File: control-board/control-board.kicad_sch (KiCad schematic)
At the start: 63 parts, among them J1 LED ch 1-24, J10 ESP32 left (3V3 row), J11 ESP32 right (GND row), J2 LED ch 25-48, J3 LED ch 49-72, J4 LED ch 73-96, J5 logic/analog, J6 24V IN, J7 24V IN (5.5/2.5), J8 FAN 24V, Q1 AO3400A, SW1 MODE, SW2 UP, SW3 DOWN, U101 PCA9685PW (0x40), U102 PCA9685PW (0x41), U103 PCA9685PW (0x42), U104 PCA9685PW (0x43), U105 PCA9685PW (0x44), U106 PCA9685PW (0x45), U110 XL1509-5.0E1, U111 ADS1115IDGS (DNP)

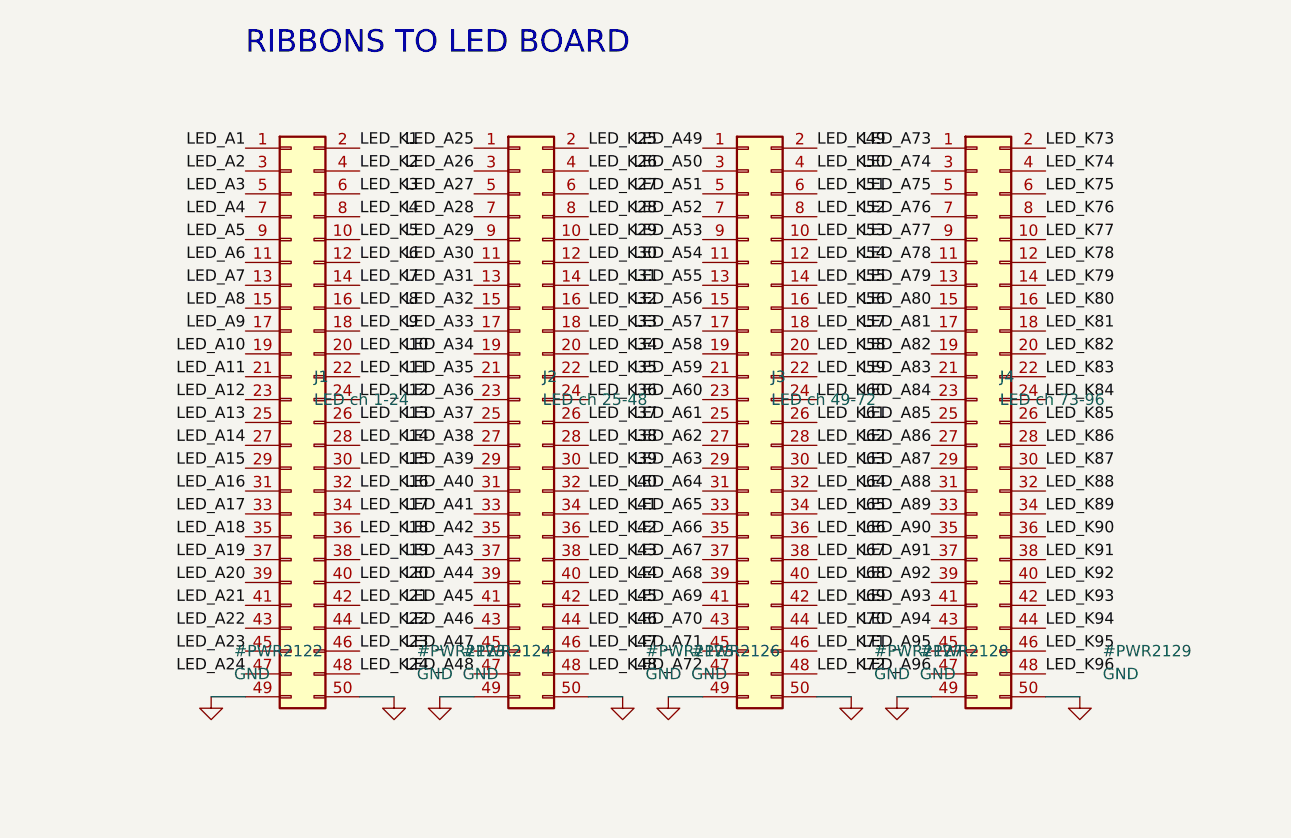
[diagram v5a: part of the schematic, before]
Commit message: Optimize ribbon/mux pin assignments to match user's PCB placement
- Quadrant mapping from actual footprint positions (via pcbnew API):
  J1 left-back = cols1-6/rows1-4, J2 right-back = cols7-12/rows1-4,
  J4 left-front = cols1-6/rows5-8, J3 right-front = cols7-12/rows5-8;
  pin pairs column-major in physical pin-1 direction (nested fan-out,
  no crossings)
- NTC->mux side-matched: U1-U3 serve cols 1-6, U6/U5/U4 cols 7-12
- pin_maps.py generated by optimize_pins.py; design_data now table-driven
- 274 labels renamed in the hand-edited LED sch (proximity-matched,
  0 misses); control board regenerated; CONNECTIONS.md updated
- Both netlists verify (300+412 nets), LED ERC still 0 errors

Co-Authored-By: Claude Fable 5 <noreply@anthropic.com>
Claude-Session: https://claude.ai/code/session_017oD54uh7Tvu54u9NPQNcZB
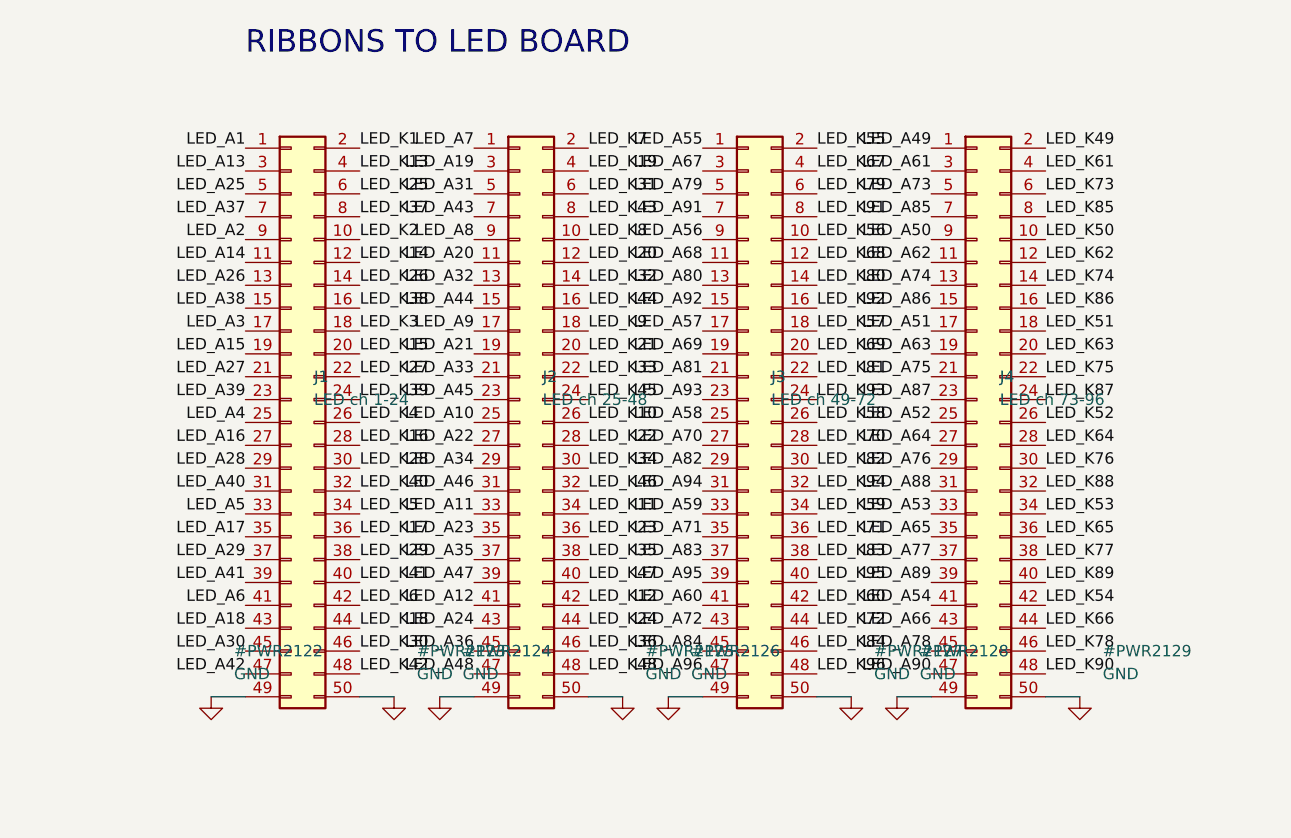
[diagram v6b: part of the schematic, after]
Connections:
- net LED_A10: now also J2.25 (Pin_25); no longer J1.19 (Pin_19)
- net LED_A11: now also J2.33 (Pin_33); no longer J1.21 (Pin_21)
- net LED_A12: now also J2.41 (Pin_41); no longer J1.23 (Pin_23)
- net LED_A13: now also J1.3 (Pin_3); no longer J1.25 (Pin_25)
- net LED_A14: now also J1.11 (Pin_11); no longer J1.27 (Pin_27)
- net LED_A15: now also J1.19 (Pin_19); no longer J1.29 (Pin_29)
- net LED_A16: now also J1.27 (Pin_27); no longer J1.31 (Pin_31)
- net LED_A17: now also J1.35 (Pin_35); no longer J1.33 (Pin_33)
- net LED_A18: now also J1.43 (Pin_43); no longer J1.35 (Pin_35)
- net LED_A19: now also J2.3 (Pin_3); no longer J1.37 (Pin_37)
- net LED_A2: now also J1.9 (Pin_9); no longer J1.3 (Pin_3)
- net LED_A20: now also J2.11 (Pin_11); no longer J1.39 (Pin_39)
- net LED_A21: now also J2.19 (Pin_19); no longer J1.41 (Pin_41)
- net LED_A22: now also J2.27 (Pin_27); no longer J1.43 (Pin_43)
- net LED_A23: now also J2.35 (Pin_35); no longer J1.45 (Pin_45)
- net LED_A24: now also J2.43 (Pin_43); no longer J1.47 (Pin_47)
- net LED_A25: now also J1.5 (Pin_5); no longer J2.1 (Pin_1)
- net LED_A26: now also J1.13 (Pin_13); no longer J2.3 (Pin_3)
- net LED_A27: now also J1.21 (Pin_21); no longer J2.5 (Pin_5)
- net LED_A28: now also J1.29 (Pin_29); no longer J2.7 (Pin_7)
- net LED_A29: now also J1.37 (Pin_37); no longer J2.9 (Pin_9)
- net LED_A3: now also J1.17 (Pin_17); no longer J1.5 (Pin_5)
- net LED_A30: now also J1.45 (Pin_45); no longer J2.11 (Pin_11)
- net LED_A31: now also J2.5 (Pin_5); no longer J2.13 (Pin_13)
- net LED_A32: now also J2.13 (Pin_13); no longer J2.15 (Pin_15)
- net LED_A33: now also J2.21 (Pin_21); no longer J2.17 (Pin_17)
- net LED_A34: now also J2.29 (Pin_29); no longer J2.19 (Pin_19)
- net LED_A35: now also J2.37 (Pin_37); no longer J2.21 (Pin_21)
- net LED_A36: now also J2.45 (Pin_45); no longer J2.23 (Pin_23)
- net LED_A37: now also J1.7 (Pin_7); no longer J2.25 (Pin_25)
- net LED_A38: now also J1.15 (Pin_15); no longer J2.27 (Pin_27)
- net LED_A39: now also J1.23 (Pin_23); no longer J2.29 (Pin_29)
- net LED_A4: now also J1.25 (Pin_25); no longer J1.7 (Pin_7)
- net LED_A40: now also J1.31 (Pin_31); no longer J2.31 (Pin_31)
- net LED_A41: now also J1.39 (Pin_39); no longer J2.33 (Pin_33)
- net LED_A42: now also J1.47 (Pin_47); no longer J2.35 (Pin_35)
- net LED_A43: now also J2.7 (Pin_7); no longer J2.37 (Pin_37)
- net LED_A44: now also J2.15 (Pin_15); no longer J2.39 (Pin_39)
- net LED_A45: now also J2.23 (Pin_23); no longer J2.41 (Pin_41)
- net LED_A46: now also J2.31 (Pin_31); no longer J2.43 (Pin_43)
- net LED_A47: now also J2.39 (Pin_39); no longer J2.45 (Pin_45)
- net LED_A49: now also J4.1 (Pin_1); no longer J3.1 (Pin_1)
- net LED_A5: now also J1.33 (Pin_33); no longer J1.9 (Pin_9)
- net LED_A50: now also J4.9 (Pin_9); no longer J3.3 (Pin_3)
- net LED_A51: now also J4.17 (Pin_17); no longer J3.5 (Pin_5)
- net LED_A52: now also J4.25 (Pin_25); no longer J3.7 (Pin_7)
- net LED_A53: now also J4.33 (Pin_33); no longer J3.9 (Pin_9)
- net LED_A54: now also J4.41 (Pin_41); no longer J3.11 (Pin_11)
- net LED_A55: now also J3.1 (Pin_1); no longer J3.13 (Pin_13)
- net LED_A56: now also J3.9 (Pin_9); no longer J3.15 (Pin_15)
- net LED_A58: now also J3.25 (Pin_25); no longer J3.19 (Pin_19)
- net LED_A59: now also J3.33 (Pin_33); no longer J3.21 (Pin_21)
- net LED_A6: now also J1.41 (Pin_41); no longer J1.11 (Pin_11)
- net LED_A60: now also J3.41 (Pin_41); no longer J3.23 (Pin_23)
- net LED_A61: now also J4.3 (Pin_3); no longer J3.25 (Pin_25)
- net LED_A62: now also J4.11 (Pin_11); no longer J3.27 (Pin_27)
- net LED_A63: now also J4.19 (Pin_19); no longer J3.29 (Pin_29)
- net LED_A64: now also J4.27 (Pin_27); no longer J3.31 (Pin_31)
- net LED_A65: now also J4.35 (Pin_35); no longer J3.33 (Pin_33)
- net LED_A66: now also J4.43 (Pin_43); no longer J3.35 (Pin_35)
- net LED_A67: now also J3.3 (Pin_3); no longer J3.37 (Pin_37)
- net LED_A68: now also J3.11 (Pin_11); no longer J3.39 (Pin_39)
- net LED_A69: now also J3.19 (Pin_19); no longer J3.41 (Pin_41)
- net LED_A7: now also J2.1 (Pin_1); no longer J1.13 (Pin_13)
- net LED_A70: now also J3.27 (Pin_27); no longer J3.43 (Pin_43)
- net LED_A71: now also J3.35 (Pin_35); no longer J3.45 (Pin_45)
- net LED_A72: now also J3.43 (Pin_43); no longer J3.47 (Pin_47)
- net LED_A73: now also J4.5 (Pin_5); no longer J4.1 (Pin_1)
- net LED_A74: now also J4.13 (Pin_13); no longer J4.3 (Pin_3)
- net LED_A75: now also J4.21 (Pin_21); no longer J4.5 (Pin_5)
- net LED_A76: now also J4.29 (Pin_29); no longer J4.7 (Pin_7)
- net LED_A77: now also J4.37 (Pin_37); no longer J4.9 (Pin_9)
- net LED_A78: now also J4.45 (Pin_45); no longer J4.11 (Pin_11)
- net LED_A79: now also J3.5 (Pin_5); no longer J4.13 (Pin_13)
- net LED_A8: now also J2.9 (Pin_9); no longer J1.15 (Pin_15)
- net LED_A80: now also J3.13 (Pin_13); no longer J4.15 (Pin_15)
- net LED_A81: now also J3.21 (Pin_21); no longer J4.17 (Pin_17)
- net LED_A82: now also J3.29 (Pin_29); no longer J4.19 (Pin_19)
- net LED_A83: now also J3.37 (Pin_37); no longer J4.21 (Pin_21)
- net LED_A84: now also J3.45 (Pin_45); no longer J4.23 (Pin_23)
- net LED_A85: now also J4.7 (Pin_7); no longer J4.25 (Pin_25)
- net LED_A86: now also J4.15 (Pin_15); no longer J4.27 (Pin_27)
- net LED_A87: now also J4.23 (Pin_23); no longer J4.29 (Pin_29)
- net LED_A89: now also J4.39 (Pin_39); no longer J4.33 (Pin_33)
- net LED_A9: now also J2.17 (Pin_17); no longer J1.17 (Pin_17)
- net LED_A90: now also J4.47 (Pin_47); no longer J4.35 (Pin_35)
- net LED_A91: now also J3.7 (Pin_7); no longer J4.37 (Pin_37)
- net LED_A92: now also J3.15 (Pin_15); no longer J4.39 (Pin_39)
- net LED_A93: now also J3.23 (Pin_23); no longer J4.41 (Pin_41)
- net LED_A94: now also J3.31 (Pin_31); no longer J4.43 (Pin_43)
- net LED_A95: now also J3.39 (Pin_39); no longer J4.45 (Pin_45)
- net LED_A96: now also J3.47 (Pin_47); no longer J4.47 (Pin_47)
- net LED_K10: now also J2.26 (Pin_26); no longer J1.20 (Pin_20)
- net LED_K11: now also J2.34 (Pin_34); no longer J1.22 (Pin_22)
- net LED_K12: now also J2.42 (Pin_42); no longer J1.24 (Pin_24)
- net LED_K13: now also J1.4 (Pin_4); no longer J1.26 (Pin_26)
- net LED_K14: now also J1.12 (Pin_12); no longer J1.28 (Pin_28)
- net LED_K15: now also J1.20 (Pin_20); no longer J1.30 (Pin_30)
- net LED_K16: now also J1.28 (Pin_28); no longer J1.32 (Pin_32)
- net LED_K17: now also J1.36 (Pin_36); no longer J1.34 (Pin_34)
- net LED_K18: now also J1.44 (Pin_44); no longer J1.36 (Pin_36)
- net LED_K19: now also J2.4 (Pin_4); no longer J1.38 (Pin_38)
- net LED_K2: now also J1.10 (Pin_10); no longer J1.4 (Pin_4)
- net LED_K20: now also J2.12 (Pin_12); no longer J1.40 (Pin_40)
- net LED_K21: now also J2.20 (Pin_20); no longer J1.42 (Pin_42)
- net LED_K22: now also J2.28 (Pin_28); no longer J1.44 (Pin_44)
- net LED_K23: now also J2.36 (Pin_36); no longer J1.46 (Pin_46)
- net LED_K24: now also J2.44 (Pin_44); no longer J1.48 (Pin_48)
- net LED_K25: now also J1.6 (Pin_6); no longer J2.2 (Pin_2)
- net LED_K26: now also J1.14 (Pin_14); no longer J2.4 (Pin_4)
- net LED_K27: now also J1.22 (Pin_22); no longer J2.6 (Pin_6)
- net LED_K28: now also J1.30 (Pin_30); no longer J2.8 (Pin_8)
- net LED_K29: now also J1.38 (Pin_38); no longer J2.10 (Pin_10)
- net LED_K3: now also J1.18 (Pin_18); no longer J1.6 (Pin_6)
- net LED_K30: now also J1.46 (Pin_46); no longer J2.12 (Pin_12)
- net LED_K31: now also J2.6 (Pin_6); no longer J2.14 (Pin_14)
- net LED_K32: now also J2.14 (Pin_14); no longer J2.16 (Pin_16)
- net LED_K33: now also J2.22 (Pin_22); no longer J2.18 (Pin_18)
- net LED_K34: now also J2.30 (Pin_30); no longer J2.20 (Pin_20)
- net LED_K35: now also J2.38 (Pin_38); no longer J2.22 (Pin_22)
- net LED_K36: now also J2.46 (Pin_46); no longer J2.24 (Pin_24)
- net LED_K37: now also J1.8 (Pin_8); no longer J2.26 (Pin_26)
- net LED_K38: now also J1.16 (Pin_16); no longer J2.28 (Pin_28)
- net LED_K39: now also J1.24 (Pin_24); no longer J2.30 (Pin_30)
- net LED_K4: now also J1.26 (Pin_26); no longer J1.8 (Pin_8)
- net LED_K40: now also J1.32 (Pin_32); no longer J2.32 (Pin_32)
- net LED_K41: now also J1.40 (Pin_40); no longer J2.34 (Pin_34)
- net LED_K42: now also J1.48 (Pin_48); no longer J2.36 (Pin_36)
- net LED_K43: now also J2.8 (Pin_8); no longer J2.38 (Pin_38)
- net LED_K44: now also J2.16 (Pin_16); no longer J2.40 (Pin_40)
- net LED_K45: now also J2.24 (Pin_24); no longer J2.42 (Pin_42)
- net LED_K46: now also J2.32 (Pin_32); no longer J2.44 (Pin_44)
- net LED_K47: now also J2.40 (Pin_40); no longer J2.46 (Pin_46)
- net LED_K49: now also J4.2 (Pin_2); no longer J3.2 (Pin_2)
- net LED_K5: now also J1.34 (Pin_34); no longer J1.10 (Pin_10)
- net LED_K50: now also J4.10 (Pin_10); no longer J3.4 (Pin_4)
- net LED_K51: now also J4.18 (Pin_18); no longer J3.6 (Pin_6)
- net LED_K52: now also J4.26 (Pin_26); no longer J3.8 (Pin_8)
- net LED_K53: now also J4.34 (Pin_34); no longer J3.10 (Pin_10)
- net LED_K54: now also J4.42 (Pin_42); no longer J3.12 (Pin_12)
- net LED_K55: now also J3.2 (Pin_2); no longer J3.14 (Pin_14)
- net LED_K56: now also J3.10 (Pin_10); no longer J3.16 (Pin_16)
- net LED_K58: now also J3.26 (Pin_26); no longer J3.20 (Pin_20)
- net LED_K59: now also J3.34 (Pin_34); no longer J3.22 (Pin_22)
- net LED_K6: now also J1.42 (Pin_42); no longer J1.12 (Pin_12)
- net LED_K60: now also J3.42 (Pin_42); no longer J3.24 (Pin_24)
- net LED_K61: now also J4.4 (Pin_4); no longer J3.26 (Pin_26)
- net LED_K62: now also J4.12 (Pin_12); no longer J3.28 (Pin_28)
- net LED_K63: now also J4.20 (Pin_20); no longer J3.30 (Pin_30)
- net LED_K64: now also J4.28 (Pin_28); no longer J3.32 (Pin_32)
- net LED_K65: now also J4.36 (Pin_36); no longer J3.34 (Pin_34)
- net LED_K66: now also J4.44 (Pin_44); no longer J3.36 (Pin_36)
- net LED_K67: now also J3.4 (Pin_4); no longer J3.38 (Pin_38)
- net LED_K68: now also J3.12 (Pin_12); no longer J3.40 (Pin_40)
- net LED_K69: now also J3.20 (Pin_20); no longer J3.42 (Pin_42)
- net LED_K7: now also J2.2 (Pin_2); no longer J1.14 (Pin_14)
- net LED_K70: now also J3.28 (Pin_28); no longer J3.44 (Pin_44)
- net LED_K71: now also J3.36 (Pin_36); no longer J3.46 (Pin_46)
- net LED_K72: now also J3.44 (Pin_44); no longer J3.48 (Pin_48)
- net LED_K73: now also J4.6 (Pin_6); no longer J4.2 (Pin_2)
- net LED_K74: now also J4.14 (Pin_14); no longer J4.4 (Pin_4)
- net LED_K75: now also J4.22 (Pin_22); no longer J4.6 (Pin_6)
- net LED_K76: now also J4.30 (Pin_30); no longer J4.8 (Pin_8)
- net LED_K77: now also J4.38 (Pin_38); no longer J4.10 (Pin_10)
- net LED_K78: now also J4.46 (Pin_46); no longer J4.12 (Pin_12)
- net LED_K79: now also J3.6 (Pin_6); no longer J4.14 (Pin_14)
- net LED_K8: now also J2.10 (Pin_10); no longer J1.16 (Pin_16)
- net LED_K80: now also J3.14 (Pin_14); no longer J4.16 (Pin_16)
- net LED_K81: now also J3.22 (Pin_22); no longer J4.18 (Pin_18)
- net LED_K82: now also J3.30 (Pin_30); no longer J4.20 (Pin_20)
- net LED_K83: now also J3.38 (Pin_38); no longer J4.22 (Pin_22)
- net LED_K84: now also J3.46 (Pin_46); no longer J4.24 (Pin_24)
- net LED_K85: now also J4.8 (Pin_8); no longer J4.26 (Pin_26)
- net LED_K86: now also J4.16 (Pin_16); no longer J4.28 (Pin_28)
- net LED_K87: now also J4.24 (Pin_24); no longer J4.30 (Pin_30)
- net LED_K89: now also J4.40 (Pin_40); no longer J4.34 (Pin_34)
- net LED_K9: now also J2.18 (Pin_18); no longer J1.18 (Pin_18)
- net LED_K90: now also J4.48 (Pin_48); no longer J4.36 (Pin_36)
- net LED_K91: now also J3.8 (Pin_8); no longer J4.38 (Pin_38)
- net LED_K92: now also J3.16 (Pin_16); no longer J4.40 (Pin_40)
- net LED_K93: now also J3.24 (Pin_24); no longer J4.42 (Pin_42)
- net LED_K94: now also J3.32 (Pin_32); no longer J4.44 (Pin_44)
- net LED_K95: now also J3.40 (Pin_40); no longer J4.46 (Pin_46)
- net LED_K96: now also J3.48 (Pin_48); no longer J4.48 (Pin_48)

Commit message: Swap to 6x 40-pin IDC ribbons (IDE-safe pinout), clear routing for rearrange
- J1-J6 both boards: 16 channels each = one PCA9685 bank per cable;
  pairs on pins 1-18/21-34, pin 20 NC (IDE key), GND 19+35-40
- Logic ribbon renamed J9; control screw terminal now J12
- Schematics regenerated (netlists verified 300+412), CONNECTIONS
  updated; connectors placed at nominal spots for user rearrangement
- All routing cleared except LED thermal via farms per user request
- New vault note: What Every Part Does

Co-Authored-By: Claude Fable 5 <noreply@anthropic.com>
Claude-Session: https://claude.ai/code/session_017oD54uh7Tvu54u9NPQNcZB
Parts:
- added J12: 24V IN, jlc_parts:TerminalBlock_KF301-5.0-2P_1x02_P5.00mm, symbol Connector:Screw_Terminal_01x02
- added J9: logic/analog, Connector_IDC:IDC-Header_2x10_P2.54mm_Horizontal, symbol Connector_Generic:Conn_02x10_Odd_Even
- J1: value LED ch 1-24 -> LED ch 1-16; footprint Connector_IDC:IDC-Header_2x25_P2.54mm_Vertical -> Connector_IDC:IDC-Header_2x20_P2.54mm_Vertical; symbol Connector_Generic:Conn_02x25_Odd_Even -> Connector_Generic:Conn_02x20_Odd_Even; LCSC C9044 -> C9043
- J2: value LED ch 25-48 -> LED ch 17-32; footprint Connector_IDC:IDC-Header_2x25_P2.54mm_Vertical -> Connector_IDC:IDC-Header_2x20_P2.54mm_Vertical; symbol Connector_Generic:Conn_02x25_Odd_Even -> Connector_Generic:Conn_02x20_Odd_Even; LCSC C9044 -> C9043
- J3: value LED ch 49-72 -> LED ch 33-48; footprint Connector_IDC:IDC-Header_2x25_P2.54mm_Vertical -> Connector_IDC:IDC-Header_2x20_P2.54mm_Vertical; symbol Connector_Generic:Conn_02x25_Odd_Even -> Connector_Generic:Conn_02x20_Odd_Even; LCSC C9044 -> C9043
- J4: value LED ch 73-96 -> LED ch 49-64; footprint Connector_IDC:IDC-Header_2x25_P2.54mm_Vertical -> Connector_IDC:IDC-Header_2x20_P2.54mm_Vertical; symbol Connector_Generic:Conn_02x25_Odd_Even -> Connector_Generic:Conn_02x20_Odd_Even; LCSC C9044 -> C9043
- J5: value logic/analog -> LED ch 65-80; footprint Connector_IDC:IDC-Header_2x10_P2.54mm_Horizontal -> Connector_IDC:IDC-Header_2x20_P2.54mm_Vertical; symbol Connector_Generic:Conn_02x10_Odd_Even -> Connector_Generic:Conn_02x20_Odd_Even; LCSC C9144 -> C9043
- J6: value 24V IN -> LED ch 81-96; footprint jlc_parts:TerminalBlock_KF301-5.0-2P_1x02_P5.00mm -> Connector_IDC:IDC-Header_2x20_P2.54mm_Vertical; symbol Connector:Screw_Terminal_01x02 -> Connector_Generic:Conn_02x20_Odd_Even; LCSC C474881 -> C9043
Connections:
- net +24V: now also J12.1 (Pin_1); no longer J6.1 (Pin_1)
- net +3.3V: now also J9.1 (Pin_1); no longer J5.1 (Pin_1)
- net GND: now also J1.19 (Pin_19), J1.35 (Pin_35), J1.36 (Pin_36), J1.37 (Pin_37), J1.38 (Pin_38), J1.39 (Pin_39), J1.40 (Pin_40), J2.19 (Pin_19), J2.35 (Pin_35), J2.36 (Pin_36), J2.37 (Pin_37), J2.38 (Pin_38), J2.39 (Pin_39), J2.40 (Pin_40), J3.19 (Pin_19), J3.35 (Pin_35), J3.36 (Pin_36), J3.37 (Pin_37), J3.38 (Pin_38), J3.39 (Pin_39), J3.40 (Pin_40), J4.19 (Pin_19), J4.35 (Pin_35), J4.36 (Pin_36), J4.37 (Pin_37), J4.38 (Pin_38), J4.39 (Pin_39), J4.40 (Pin_40), J5.35 (Pin_35), J5.36 (Pin_36), J5.37 (Pin_37), J5.38 (Pin_38), J5.39 (Pin_39), J5.40 (Pin_40), J6.19 (Pin_19), J6.35 (Pin_35), J6.36 (Pin_36), J6.37 (Pin_37), J6.38 (Pin_38), J6.39 (Pin_39), J6.40 (Pin_40), J12.2 (Pin_2), J9.10 (Pin_10), J9.12 (Pin_12), J9.14 (Pin_14), J9.19 (Pin_19), J9.2 (Pin_2), J9.20 (Pin_20), J9.4 (Pin_4), J9.6 (Pin_6), J9.8 (Pin_8); no longer J1.49 (Pin_49), J1.50 (Pin_50), J2.49 (Pin_49), J2.50 (Pin_50), J3.49 (Pin_49), J3.50 (Pin_50), J4.49 (Pin_49), J4.50 (Pin_50), J5.10 (Pin_10), J5.12 (Pin_12), J5.14 (Pin_14), J5.2 (Pin_2), J5.20 (Pin_20), J5.4 (Pin_4), J5.6 (Pin_6), J5.8 (Pin_8), J6.2 (Pin_2)
- net LED_A10: now also J1.21 (Pin_21); no longer J2.25 (Pin_25)
- net LED_A11: now also J1.23 (Pin_23); no longer J2.33 (Pin_33)
- net LED_A12: now also J1.25 (Pin_25); no longer J2.41 (Pin_41)
- net LED_A13: now also J1.27 (Pin_27); no longer J1.3 (Pin_3)
- net LED_A14: now also J1.29 (Pin_29); no longer J1.11 (Pin_11)
- net LED_A15: now also J1.31 (Pin_31); no longer J1.19 (Pin_19)
- net LED_A16: now also J1.33 (Pin_33); no longer J1.27 (Pin_27)
- net LED_A17: now also J2.1 (Pin_1); no longer J1.35 (Pin_35)
- net LED_A18: now also J2.3 (Pin_3); no longer J1.43 (Pin_43)
- net LED_A19: now also J2.5 (Pin_5); no longer J2.3 (Pin_3)
- net LED_A2: now also J1.3 (Pin_3); no longer J1.9 (Pin_9)
- net LED_A20: now also J2.7 (Pin_7); no longer J2.11 (Pin_11)
- net LED_A21: now also J2.9 (Pin_9); no longer J2.19 (Pin_19)
- net LED_A22: now also J2.11 (Pin_11); no longer J2.27 (Pin_27)
- net LED_A23: now also J2.13 (Pin_13); no longer J2.35 (Pin_35)
- net LED_A24: now also J2.15 (Pin_15); no longer J2.43 (Pin_43)
- net LED_A25: now also J2.17 (Pin_17); no longer J1.5 (Pin_5)
- net LED_A26: now also J2.21 (Pin_21); no longer J1.13 (Pin_13)
- net LED_A27: now also J2.23 (Pin_23); no longer J1.21 (Pin_21)
- net LED_A28: now also J2.25 (Pin_25); no longer J1.29 (Pin_29)
- net LED_A29: now also J2.27 (Pin_27); no longer J1.37 (Pin_37)
- net LED_A3: now also J1.5 (Pin_5); no longer J1.17 (Pin_17)
- net LED_A30: now also J2.29 (Pin_29); no longer J1.45 (Pin_45)
- net LED_A31: now also J2.31 (Pin_31); no longer J2.5 (Pin_5)
- net LED_A32: now also J2.33 (Pin_33); no longer J2.13 (Pin_13)
- net LED_A33: now also J3.1 (Pin_1); no longer J2.21 (Pin_21)
- net LED_A34: now also J3.3 (Pin_3); no longer J2.29 (Pin_29)
- net LED_A35: now also J3.5 (Pin_5); no longer J2.37 (Pin_37)
- net LED_A36: now also J3.7 (Pin_7); no longer J2.45 (Pin_45)
- net LED_A37: now also J3.9 (Pin_9); no longer J1.7 (Pin_7)
- net LED_A38: now also J3.11 (Pin_11); no longer J1.15 (Pin_15)
- net LED_A39: now also J3.13 (Pin_13); no longer J1.23 (Pin_23)
- net LED_A4: now also J1.7 (Pin_7); no longer J1.25 (Pin_25)
- net LED_A40: now also J3.15 (Pin_15); no longer J1.31 (Pin_31)
- net LED_A41: now also J3.17 (Pin_17); no longer J1.39 (Pin_39)
- net LED_A42: now also J3.21 (Pin_21); no longer J1.47 (Pin_47)
- net LED_A43: now also J3.23 (Pin_23); no longer J2.7 (Pin_7)
- net LED_A44: now also J3.25 (Pin_25); no longer J2.15 (Pin_15)
- net LED_A45: now also J3.27 (Pin_27); no longer J2.23 (Pin_23)
- net LED_A46: now also J3.29 (Pin_29); no longer J2.31 (Pin_31)
- net LED_A47: now also J3.31 (Pin_31); no longer J2.39 (Pin_39)
- net LED_A48: now also J3.33 (Pin_33); no longer J2.47 (Pin_47)
- net LED_A5: now also J1.9 (Pin_9); no longer J1.33 (Pin_33)
- net LED_A50: now also J4.3 (Pin_3); no longer J4.9 (Pin_9)
- net LED_A51: now also J4.5 (Pin_5); no longer J4.17 (Pin_17)
- net LED_A52: now also J4.7 (Pin_7); no longer J4.25 (Pin_25)
- net LED_A53: now also J4.9 (Pin_9); no longer J4.33 (Pin_33)
- net LED_A54: now also J4.11 (Pin_11); no longer J4.41 (Pin_41)
- net LED_A55: now also J4.13 (Pin_13); no longer J3.1 (Pin_1)
- net LED_A56: now also J4.15 (Pin_15); no longer J3.9 (Pin_9)
- net LED_A57: now also J4.17 (Pin_17); no longer J3.17 (Pin_17)
- net LED_A58: now also J4.21 (Pin_21); no longer J3.25 (Pin_25)
- net LED_A59: now also J4.23 (Pin_23); no longer J3.33 (Pin_33)
- net LED_A6: now also J1.11 (Pin_11); no longer J1.41 (Pin_41)
- net LED_A60: now also J4.25 (Pin_25); no longer J3.41 (Pin_41)
- net LED_A61: now also J4.27 (Pin_27); no longer J4.3 (Pin_3)
- net LED_A62: now also J4.29 (Pin_29); no longer J4.11 (Pin_11)
- net LED_A63: now also J4.31 (Pin_31); no longer J4.19 (Pin_19)
- net LED_A64: now also J4.33 (Pin_33); no longer J4.27 (Pin_27)
- net LED_A65: now also J5.1 (Pin_1); no longer J4.35 (Pin_35)
- net LED_A66: now also J5.3 (Pin_3); no longer J4.43 (Pin_43)
- net LED_A67: now also J5.5 (Pin_5); no longer J3.3 (Pin_3)
- net LED_A68: now also J5.7 (Pin_7); no longer J3.11 (Pin_11)
- net LED_A69: now also J5.9 (Pin_9); no longer J3.19 (Pin_19)
- net LED_A7: now also J1.13 (Pin_13); no longer J2.1 (Pin_1)
- net LED_A70: now also J5.11 (Pin_11); no longer J3.27 (Pin_27)
- net LED_A71: now also J5.13 (Pin_13); no longer J3.35 (Pin_35)
- net LED_A72: now also J5.15 (Pin_15); no longer J3.43 (Pin_43)
- net LED_A73: now also J5.17 (Pin_17); no longer J4.5 (Pin_5)
- net LED_A74: now also J5.21 (Pin_21); no longer J4.13 (Pin_13)
- net LED_A75: now also J5.23 (Pin_23); no longer J4.21 (Pin_21)
- net LED_A76: now also J5.25 (Pin_25); no longer J4.29 (Pin_29)
- net LED_A77: now also J5.27 (Pin_27); no longer J4.37 (Pin_37)
- net LED_A78: now also J5.29 (Pin_29); no longer J4.45 (Pin_45)
- net LED_A79: now also J5.31 (Pin_31); no longer J3.5 (Pin_5)
- net LED_A8: now also J1.15 (Pin_15); no longer J2.9 (Pin_9)
- net LED_A80: now also J5.33 (Pin_33); no longer J3.13 (Pin_13)
- net LED_A81: now also J6.1 (Pin_1); no longer J3.21 (Pin_21)
- net LED_A82: now also J6.3 (Pin_3); no longer J3.29 (Pin_29)
- net LED_A83: now also J6.5 (Pin_5); no longer J3.37 (Pin_37)
- net LED_A84: now also J6.7 (Pin_7); no longer J3.45 (Pin_45)
- net LED_A85: now also J6.9 (Pin_9); no longer J4.7 (Pin_7)
- net LED_A86: now also J6.11 (Pin_11); no longer J4.15 (Pin_15)
- net LED_A87: now also J6.13 (Pin_13); no longer J4.23 (Pin_23)
- net LED_A88: now also J6.15 (Pin_15); no longer J4.31 (Pin_31)
- net LED_A89: now also J6.17 (Pin_17); no longer J4.39 (Pin_39)
- net LED_A9: now also J1.17 (Pin_17); no longer J2.17 (Pin_17)
- net LED_A90: now also J6.21 (Pin_21); no longer J4.47 (Pin_47)
- net LED_A91: now also J6.23 (Pin_23); no longer J3.7 (Pin_7)
- net LED_A92: now also J6.25 (Pin_25); no longer J3.15 (Pin_15)
- net LED_A93: now also J6.27 (Pin_27); no longer J3.23 (Pin_23)
- net LED_A94: now also J6.29 (Pin_29); no longer J3.31 (Pin_31)
- net LED_A95: now also J6.31 (Pin_31); no longer J3.39 (Pin_39)
- net LED_A96: now also J6.33 (Pin_33); no longer J3.47 (Pin_47)
- net LED_K10: now also J1.22 (Pin_22); no longer J2.26 (Pin_26)
- net LED_K11: now also J1.24 (Pin_24); no longer J2.34 (Pin_34)
- net LED_K12: now also J1.26 (Pin_26); no longer J2.42 (Pin_42)
- net LED_K13: now also J1.28 (Pin_28); no longer J1.4 (Pin_4)
- net LED_K14: now also J1.30 (Pin_30); no longer J1.12 (Pin_12)
- net LED_K15: now also J1.32 (Pin_32); no longer J1.20 (Pin_20)
- net LED_K16: now also J1.34 (Pin_34); no longer J1.28 (Pin_28)
- net LED_K17: now also J2.2 (Pin_2); no longer J1.36 (Pin_36)
- net LED_K18: now also J2.4 (Pin_4); no longer J1.44 (Pin_44)
- net LED_K19: now also J2.6 (Pin_6); no longer J2.4 (Pin_4)
- net LED_K2: now also J1.4 (Pin_4); no longer J1.10 (Pin_10)
- net LED_K20: now also J2.8 (Pin_8); no longer J2.12 (Pin_12)
- net LED_K21: now also J2.10 (Pin_10); no longer J2.20 (Pin_20)
- net LED_K22: now also J2.12 (Pin_12); no longer J2.28 (Pin_28)
- net LED_K23: now also J2.14 (Pin_14); no longer J2.36 (Pin_36)
- net LED_K24: now also J2.16 (Pin_16); no longer J2.44 (Pin_44)
- net LED_K25: now also J2.18 (Pin_18); no longer J1.6 (Pin_6)
- net LED_K26: now also J2.22 (Pin_22); no longer J1.14 (Pin_14)
- net LED_K27: now also J2.24 (Pin_24); no longer J1.22 (Pin_22)
- net LED_K28: now also J2.26 (Pin_26); no longer J1.30 (Pin_30)
- net LED_K29: now also J2.28 (Pin_28); no longer J1.38 (Pin_38)
- net LED_K3: now also J1.6 (Pin_6); no longer J1.18 (Pin_18)
- net LED_K30: now also J2.30 (Pin_30); no longer J1.46 (Pin_46)
- net LED_K31: now also J2.32 (Pin_32); no longer J2.6 (Pin_6)
- net LED_K32: now also J2.34 (Pin_34); no longer J2.14 (Pin_14)
- net LED_K33: now also J3.2 (Pin_2); no longer J2.22 (Pin_22)
- net LED_K34: now also J3.4 (Pin_4); no longer J2.30 (Pin_30)
- net LED_K35: now also J3.6 (Pin_6); no longer J2.38 (Pin_38)
- net LED_K36: now also J3.8 (Pin_8); no longer J2.46 (Pin_46)
- net LED_K37: now also J3.10 (Pin_10); no longer J1.8 (Pin_8)
- net LED_K38: now also J3.12 (Pin_12); no longer J1.16 (Pin_16)
- net LED_K39: now also J3.14 (Pin_14); no longer J1.24 (Pin_24)
- net LED_K4: now also J1.8 (Pin_8); no longer J1.26 (Pin_26)
- net LED_K40: now also J3.16 (Pin_16); no longer J1.32 (Pin_32)
- net LED_K41: now also J3.18 (Pin_18); no longer J1.40 (Pin_40)
- net LED_K42: now also J3.22 (Pin_22); no longer J1.48 (Pin_48)
- net LED_K43: now also J3.24 (Pin_24); no longer J2.8 (Pin_8)
- net LED_K44: now also J3.26 (Pin_26); no longer J2.16 (Pin_16)
- net LED_K45: now also J3.28 (Pin_28); no longer J2.24 (Pin_24)
- net LED_K46: now also J3.30 (Pin_30); no longer J2.32 (Pin_32)
- net LED_K47: now also J3.32 (Pin_32); no longer J2.40 (Pin_40)
- net LED_K48: now also J3.34 (Pin_34); no longer J2.48 (Pin_48)
- net LED_K5: now also J1.10 (Pin_10); no longer J1.34 (Pin_34)
- net LED_K50: now also J4.4 (Pin_4); no longer J4.10 (Pin_10)
- net LED_K51: now also J4.6 (Pin_6); no longer J4.18 (Pin_18)
- net LED_K52: now also J4.8 (Pin_8); no longer J4.26 (Pin_26)
- net LED_K53: now also J4.10 (Pin_10); no longer J4.34 (Pin_34)
- net LED_K54: now also J4.12 (Pin_12); no longer J4.42 (Pin_42)
- net LED_K55: now also J4.14 (Pin_14); no longer J3.2 (Pin_2)
- net LED_K56: now also J4.16 (Pin_16); no longer J3.10 (Pin_10)
- net LED_K57: now also J4.18 (Pin_18); no longer J3.18 (Pin_18)
- net LED_K58: now also J4.22 (Pin_22); no longer J3.26 (Pin_26)
- net LED_K59: now also J4.24 (Pin_24); no longer J3.34 (Pin_34)
- net LED_K6: now also J1.12 (Pin_12); no longer J1.42 (Pin_42)
- net LED_K60: now also J4.26 (Pin_26); no longer J3.42 (Pin_42)
- net LED_K61: now also J4.28 (Pin_28); no longer J4.4 (Pin_4)
- net LED_K62: now also J4.30 (Pin_30); no longer J4.12 (Pin_12)
- net LED_K63: now also J4.32 (Pin_32); no longer J4.20 (Pin_20)
- net LED_K64: now also J4.34 (Pin_34); no longer J4.28 (Pin_28)
- net LED_K65: now also J5.2 (Pin_2); no longer J4.36 (Pin_36)
- net LED_K66: now also J5.4 (Pin_4); no longer J4.44 (Pin_44)
- net LED_K67: now also J5.6 (Pin_6); no longer J3.4 (Pin_4)
- net LED_K68: now also J5.8 (Pin_8); no longer J3.12 (Pin_12)
- net LED_K69: now also J5.10 (Pin_10); no longer J3.20 (Pin_20)
- net LED_K7: now also J1.14 (Pin_14); no longer J2.2 (Pin_2)
- net LED_K70: now also J5.12 (Pin_12); no longer J3.28 (Pin_28)
- net LED_K71: now also J5.14 (Pin_14); no longer J3.36 (Pin_36)
- net LED_K72: now also J5.16 (Pin_16); no longer J3.44 (Pin_44)
- net LED_K73: now also J5.18 (Pin_18); no longer J4.6 (Pin_6)
- net LED_K74: now also J5.22 (Pin_22); no longer J4.14 (Pin_14)
- net LED_K75: now also J5.24 (Pin_24); no longer J4.22 (Pin_22)
- net LED_K76: now also J5.26 (Pin_26); no longer J4.30 (Pin_30)
- net LED_K77: now also J5.28 (Pin_28); no longer J4.38 (Pin_38)
- net LED_K78: now also J5.30 (Pin_30); no longer J4.46 (Pin_46)
- net LED_K79: now also J5.32 (Pin_32); no longer J3.6 (Pin_6)
- net LED_K8: now also J1.16 (Pin_16); no longer J2.10 (Pin_10)
- net LED_K80: now also J5.34 (Pin_34); no longer J3.14 (Pin_14)
- net LED_K81: now also J6.2 (Pin_2); no longer J3.22 (Pin_22)
- net LED_K82: now also J6.4 (Pin_4); no longer J3.30 (Pin_30)
- net LED_K83: now also J6.6 (Pin_6); no longer J3.38 (Pin_38)
- net LED_K84: now also J6.8 (Pin_8); no longer J3.46 (Pin_46)
- net LED_K85: now also J6.10 (Pin_10); no longer J4.8 (Pin_8)
- net LED_K86: now also J6.12 (Pin_12); no longer J4.16 (Pin_16)
- net LED_K87: now also J6.14 (Pin_14); no longer J4.24 (Pin_24)
- net LED_K88: now also J6.16 (Pin_16); no longer J4.32 (Pin_32)
- net LED_K89: now also J6.18 (Pin_18); no longer J4.40 (Pin_40)
- net LED_K9: now also J1.18 (Pin_18); no longer J2.18 (Pin_18)
- net LED_K90: now also J6.22 (Pin_22); no longer J4.48 (Pin_48)
- net LED_K91: now also J6.24 (Pin_24); no longer J3.8 (Pin_8)
- net LED_K92: now also J6.26 (Pin_26); no longer J3.16 (Pin_16)
- net LED_K93: now also J6.28 (Pin_28); no longer J3.24 (Pin_24)
- net LED_K94: now also J6.30 (Pin_30); no longer J3.32 (Pin_32)
- net LED_K95: now also J6.32 (Pin_32); no longer J3.40 (Pin_40)
- net LED_K96: now also J6.34 (Pin_34); no longer J3.48 (Pin_48)
- net MUX_A0: now also J9.15 (Pin_15); no longer J5.15 (Pin_15)
- net MUX_A1: now also J9.16 (Pin_16); no longer J5.16 (Pin_16)
- net MUX_A2: now also J9.17 (Pin_17); no longer J5.17 (Pin_17)
- net MUX_A3: now also J9.18 (Pin_18); no longer J5.18 (Pin_18)
- net NTC_SIG1: now also J9.3 (Pin_3); no longer J5.3 (Pin_3)
- net NTC_SIG2: now also J9.5 (Pin_5); no longer J5.5 (Pin_5)
- net NTC_SIG3: now also J9.7 (Pin_7); no longer J5.7 (Pin_7)
- net NTC_SIG4: now also J9.9 (Pin_9); no longer J5.9 (Pin_9)
- net NTC_SIG5: now also J9.11 (Pin_11); no longer J5.11 (Pin_11)
- net NTC_SIG6: now also J9.13 (Pin_13); no longer J5.13 (Pin_13)
- no-connect marks 20 -> 26
